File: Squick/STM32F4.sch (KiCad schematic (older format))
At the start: 18 parts

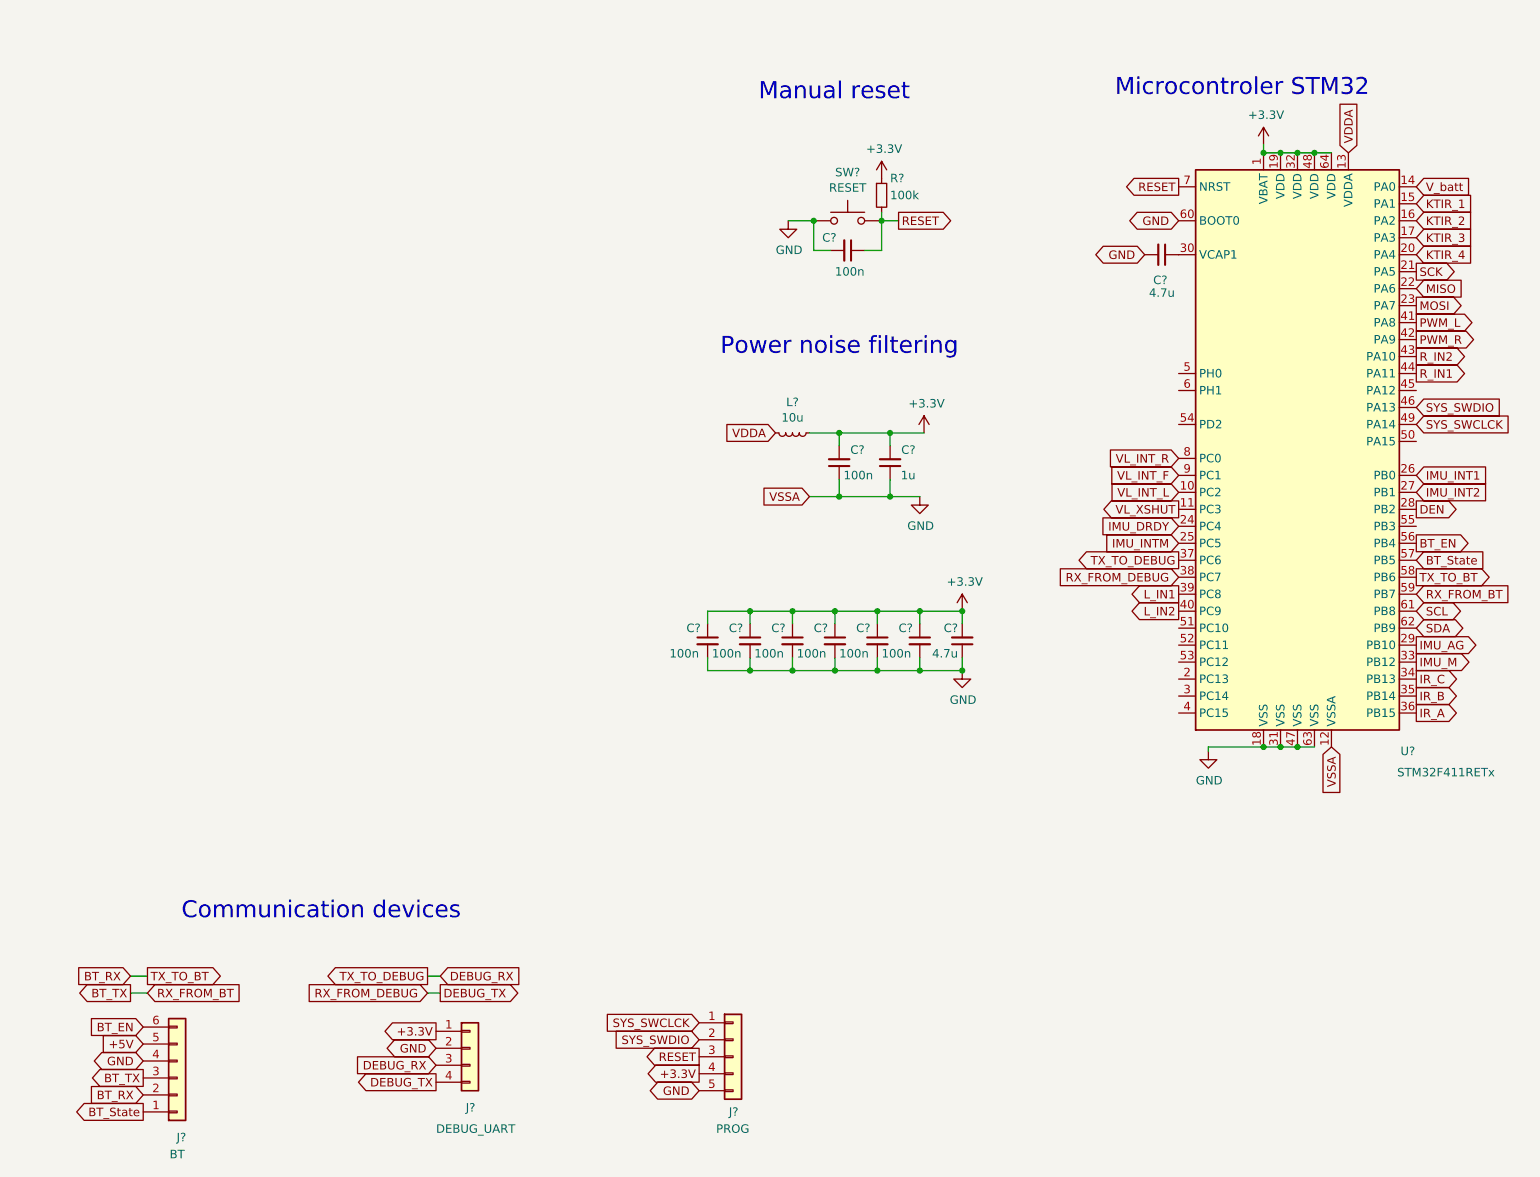
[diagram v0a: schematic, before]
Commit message: Finished electrical scheme
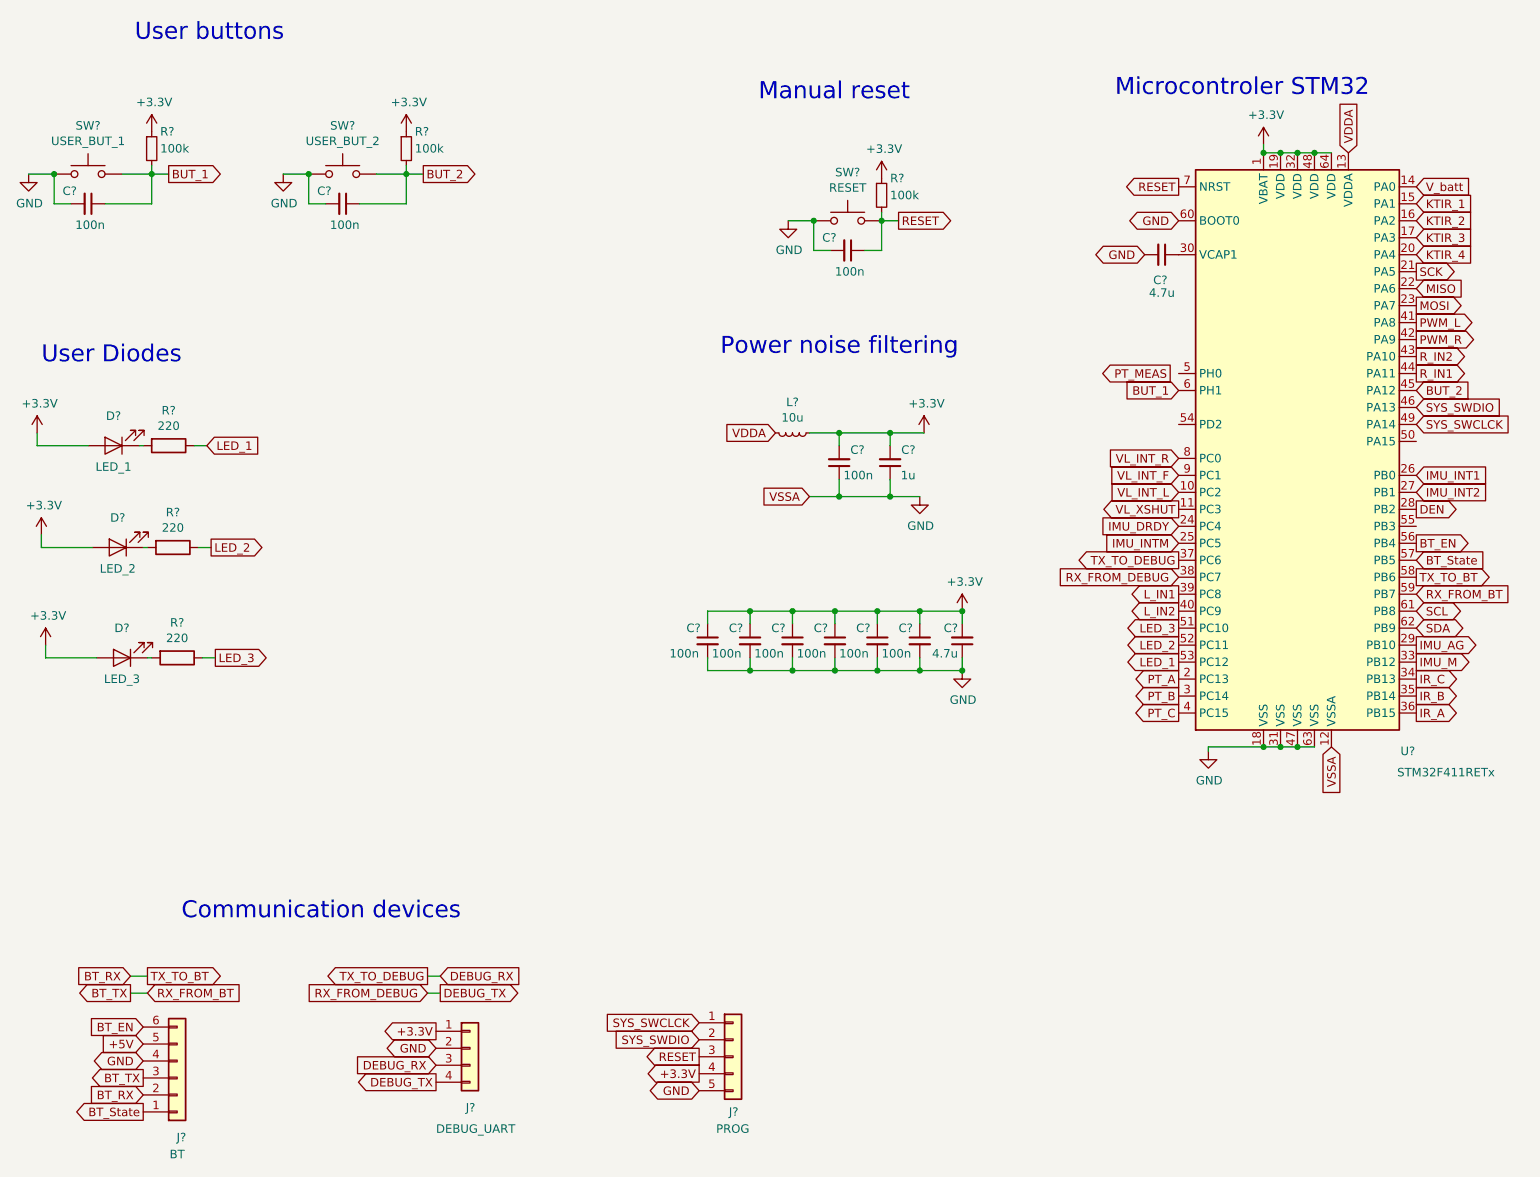
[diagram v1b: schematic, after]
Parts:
- added C? (x2): 100n, symbol Device:C_Small
- added D?: LED_1, symbol Device:LED
- added D?: LED_2, symbol Device:LED
- added D?: LED_3, symbol Device:LED
- added R? (x2): 100k, symbol Device:R_Small
- added R? (x3): 220, symbol Device:R
- added SW?: USER_BUT_1, symbol Switch:SW_Push
- added SW?: USER_BUT_2, symbol Switch:SW_Push
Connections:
- net +3V3: now also D?.2 (A), D?.2 (A), D?.2 (A), R?.1, R?.1
- net GND: now also C?.2, C?.2, SW?.1, SW?.1
- net PT_A: now reaches U?.2 (PC13)
- net PT_B: now reaches U?.3 (PC14)
- net PT_C: now reaches U?.4 (PC15)
- net BUT_2: now reaches U?.45 (PA12)
- net BUT_2: now also C?.1, R?.2, SW?.2
- net LED_3: now reaches U?.51 (PC10)
- net LED_3: now also R?.1
- net LED_2: now reaches U?.52 (PC11)
- net LED_2: now also R?.1
- net LED_1: now reaches U?.53 (PC12)
- net LED_1: now also R?.1
- net BUT_1: now reaches U?.6 (PH1)
- net BUT_1: now also C?.1, R?.2, SW?.2
- new net: D?.1 (K), R?.2 (x3)
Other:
- note added: "User Diodes\n"
- note added: "User buttons"
